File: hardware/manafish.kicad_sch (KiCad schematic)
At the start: 1 part, among them J6 Battery

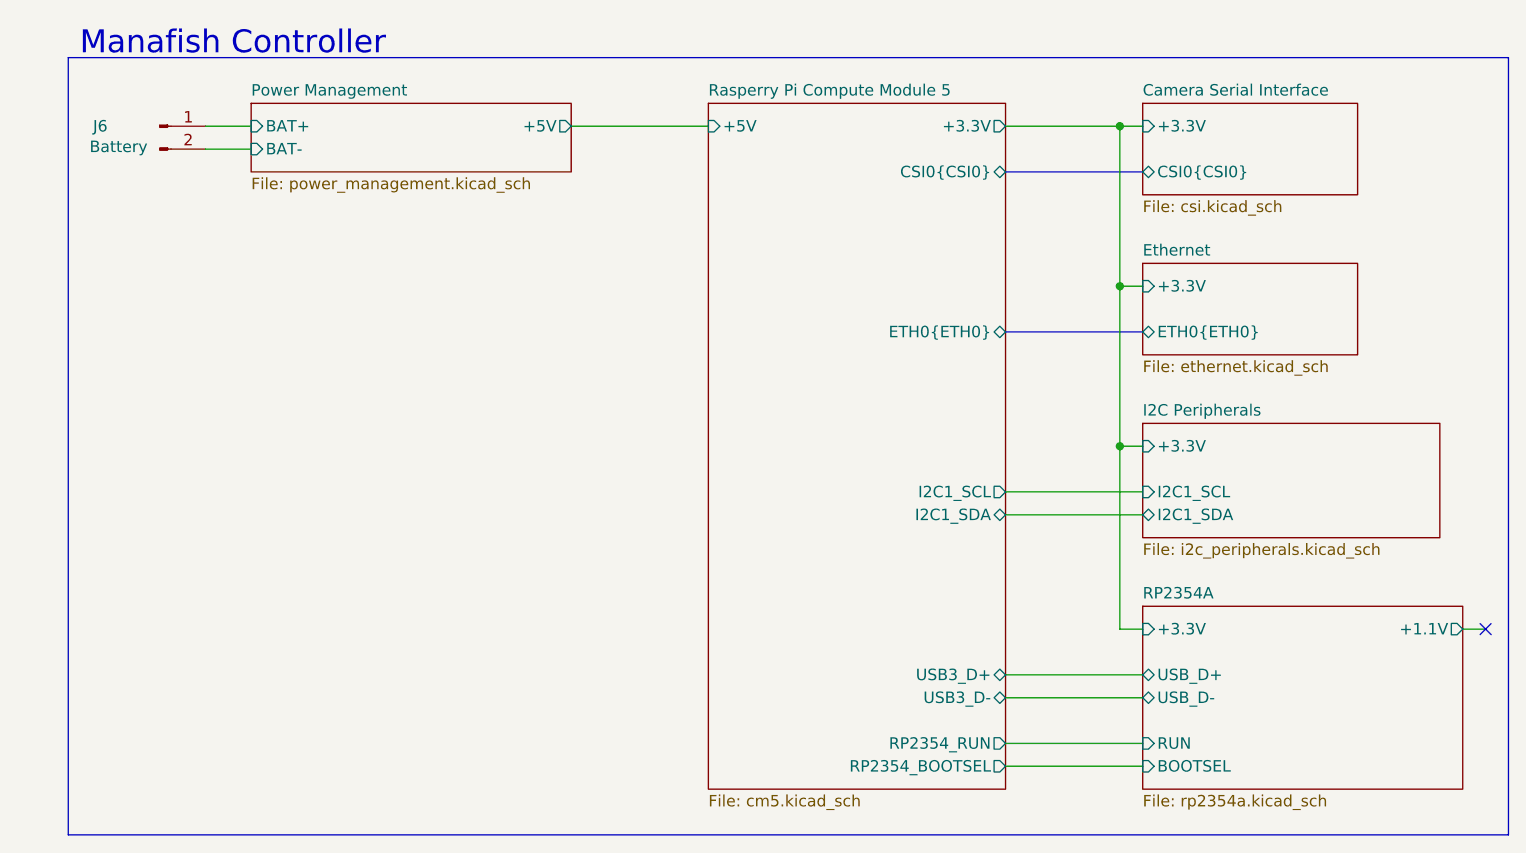
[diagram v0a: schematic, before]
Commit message: Fix schematic connectivity and add flashing access
The camera and Ethernet buses now connect across sheets: they use
unnamed bus groups so the member nets keep their names. Ethernet pair 2
negative is no longer tied to GND.

The RP2354A core supply reaches the regulator output, and a 12 MHz
crystal drives XIN/XOUT, which USB and the USB bootloader need. The
CM5 gets GPIO_VREF on 3.3 V, the IO Board's boot and EEPROM jumper
header, and a data-only USB-C port with 5.1 kOhm CC resistors for
flashing the eMMC.

Co-Authored-By: Claude Opus 5.5 <noreply@anthropic.com>
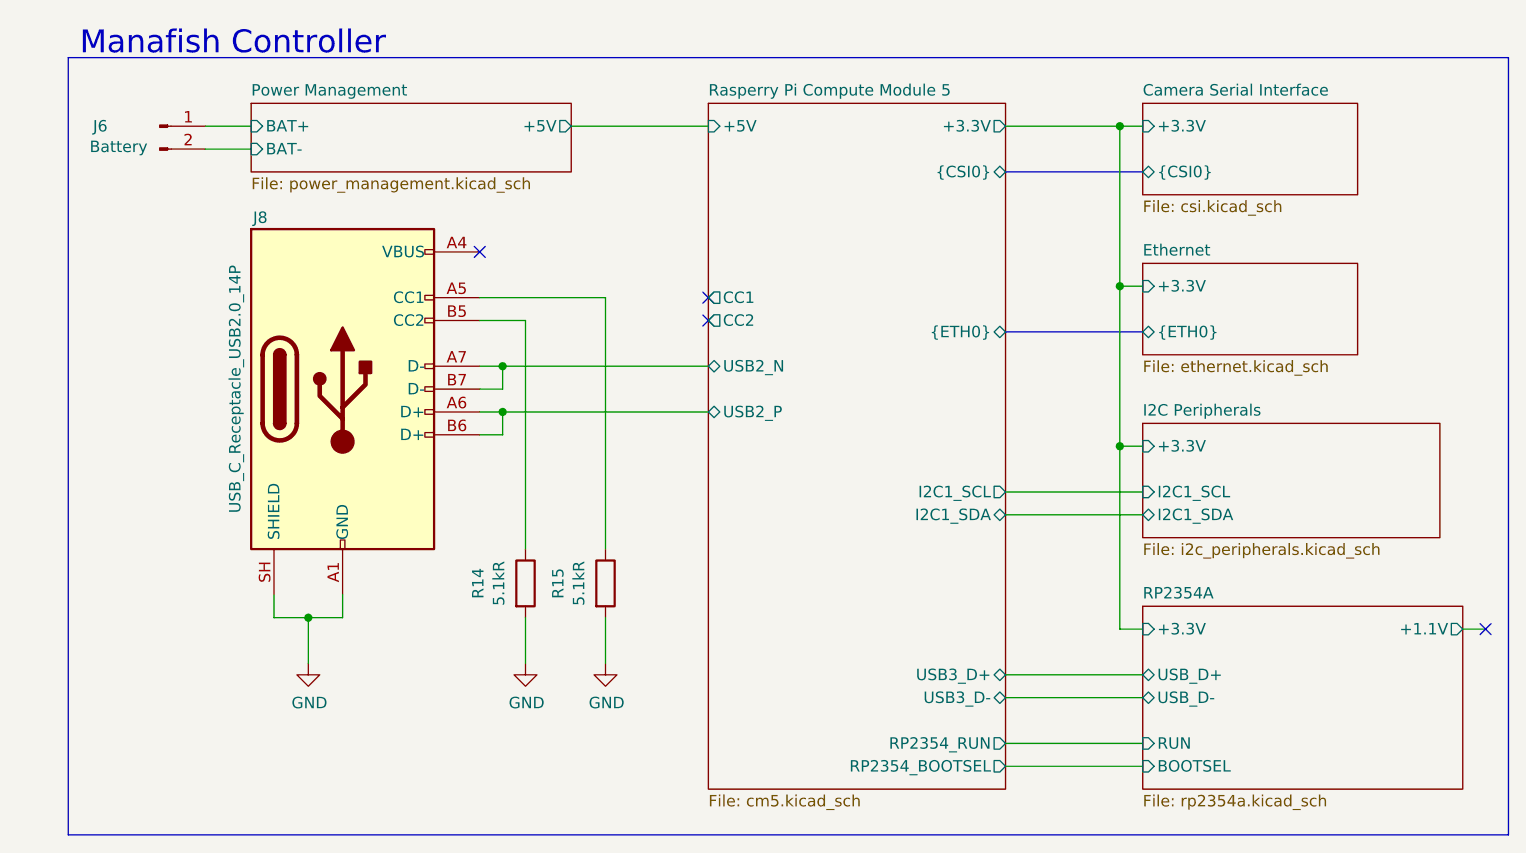
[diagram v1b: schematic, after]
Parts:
- added J8: USB_C_Receptacle_USB2.0_14P, symbol Connector:USB_C_Receptacle_USB2.0_14P
- added R14, R15: 5.1kR, Resistor_SMD:R_0402_1005Metric, symbol Device:R
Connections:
- new net: J8.A4 (VBUS), J8.A9 (VBUS), J8.B4 (VBUS), J8.B9 (VBUS)
- new net: J8.A5 (CC1), R15.1
- new net: J8.B5 (CC2), R14.1
- new net GND: J8.A1 (GND), J8.A12 (GND), J8.B1 (GND), J8.B12 (GND), J8.SH (SHIELD), R14.2, R15.2
- new net Rasperry Pi Compute Module 5/USB2_N: J8.A7 (D-), J8.B7 (D-)
- new net Rasperry Pi Compute Module 5/USB2_P: J8.A6 (D+), J8.B6 (D+)
- no-connect marks 1 -> 4
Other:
- sheet Camera Serial Interface ports: added {CSI0}; removed CSI0{CSI0}
- sheet Ethernet ports: added {ETH0}; removed ETH0{ETH0}
- sheet Rasperry Pi Compute Module 5 ports: added CC1, CC2, USB2_N, USB2_P, {CSI0}, {ETH0}; removed CSI0{CSI0}, ETH0{ETH0}

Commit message: Assign footprints to all parts
Connectors get footprints for the chosen hardware: JST GH for the ESC
and pressure-sensor cables, XT30 for the battery and the GCT USB4105
for the service port. The core regulator inductor and the SWD
connector use the footprints from Raspberry Pi's RP2350A minimal
design, which is MIT-licensed and credited in NOTICE.md. Every symbol
pin now has a matching pad.

Co-Authored-By: Claude Opus 5.5 <noreply@anthropic.com>
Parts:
- J6: footprint (none) -> Connector_AMASS:AMASS_XT30PW-M_1x02_P2.50mm_Horizontal
- J8: footprint (none) -> Connector_USB:USB_C_Receptacle_GCT_USB4105-xx-A_16P_TopMnt_Horizontal
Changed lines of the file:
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@@
 			)
 		)
-		(property "Footprint" ""
+		(property "Footprint" "Connector_USB:USB_C_Receptacle_GCT_USB4105-xx-A_16P_TopMnt_Horizontal"
 			(at 49.53 54.61 0)
 			(hide yes)
@@
 			)
 		)
-		(property "Footprint" ""
+		(property "Footprint" "Connector_AMASS:AMASS_XT30PW-M_1x02_P2.50mm_Horizontal"
 			(at 25.4 25.4 0)
 			(hide yes)
